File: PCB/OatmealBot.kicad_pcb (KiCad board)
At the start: 2 copper layers, 65 x 56 mm, 12 parts, among them J2 RPi_GPIO, J5 Motor 3, J6 Motor 4, J8 Motor 1, J9 Motor 2, U2 SPI_OLED, U3 FTDI-Cable, U4 PololuD24V22F

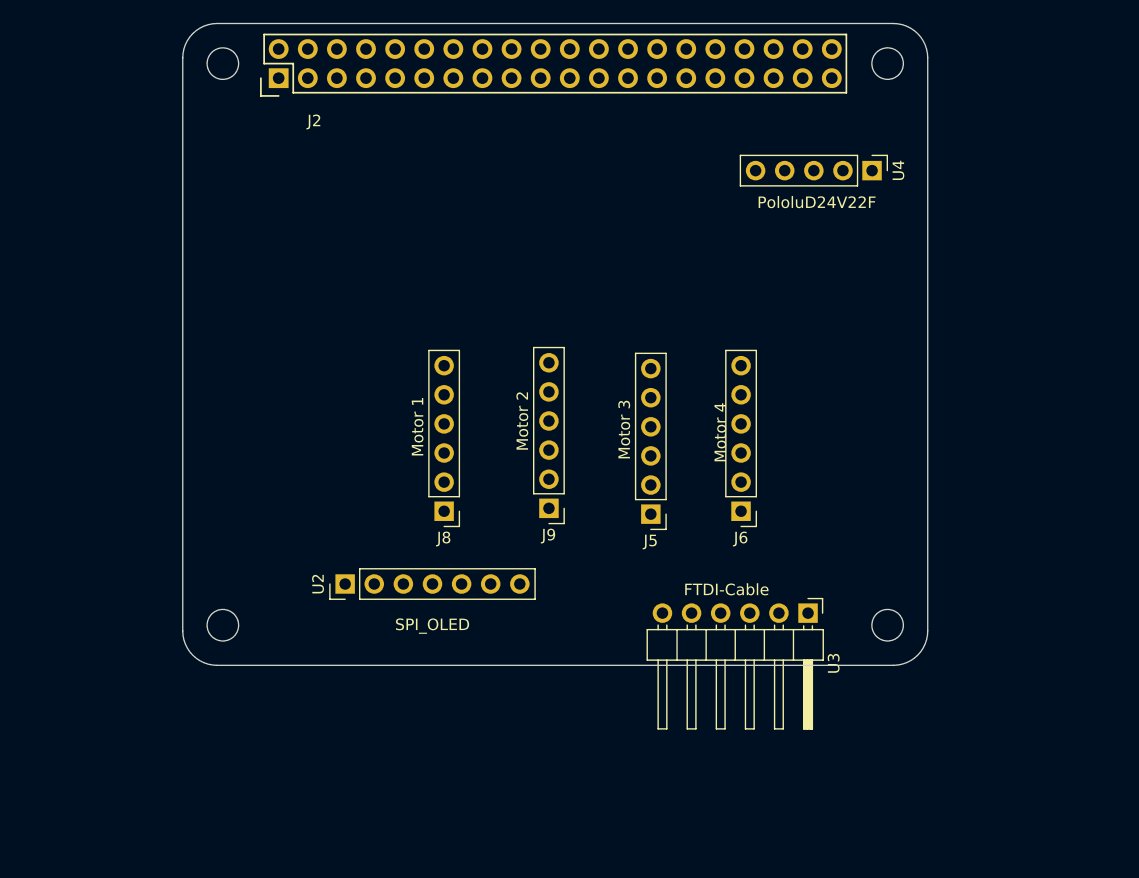
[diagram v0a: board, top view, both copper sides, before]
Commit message: Updated to KiCad 4.0.7 (which lost the 3D models I had just gotten working) Assigned more footprints.
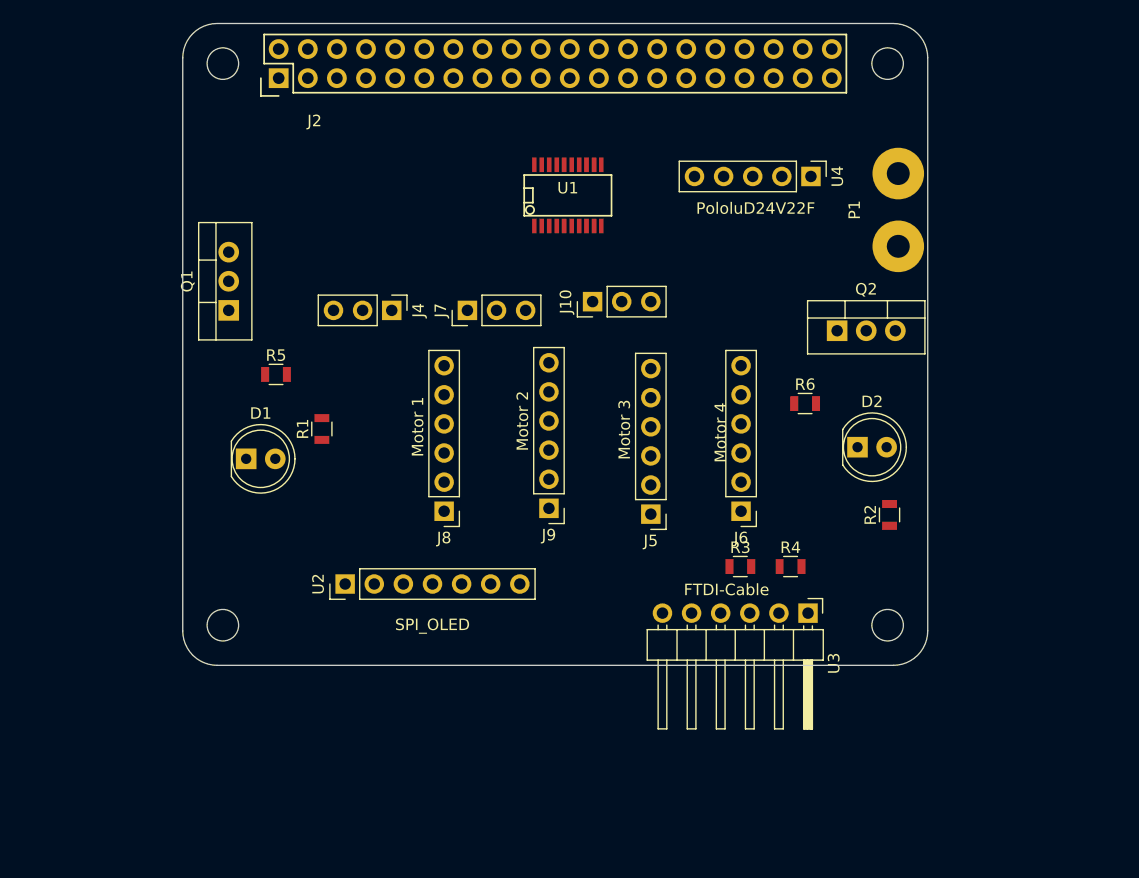
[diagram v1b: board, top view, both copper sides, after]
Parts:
- added D1: LED, LEDs:LED_D5.0mm, F.Cu at (18.0, 62.5)
- added D2: LED, LEDs:LED_D5.0mm, F.Cu at (71.4, 61.5)
- added J10: ServoHeader3, Pin_Headers:Pin_Header_Straight_1x03_Pitch2.54mm, F.Cu at (48.3, 48.8)
- added J4: ServoHeader1, Pin_Headers:Pin_Header_Straight_1x03_Pitch2.54mm, F.Cu at (30.7, 49.5)
- added J7: ServoHeader2, Pin_Headers:Pin_Header_Straight_1x03_Pitch2.54mm, F.Cu at (37.3, 49.5)
- added P1: Motor Hat Power, Wire_Pads:SolderWirePad_2x_2mmDrill, F.Cu at (74.9, 40.8)
- added Q1: STP55NF06L, TO_SOT_Packages_THT:TO-220-3_Vertical, F.Cu at (16.5, 49.5)
- added Q2: STP55NF06L, TO_SOT_Packages_THT:TO-220-3_Vertical, F.Cu at (69.6, 51.3)
- added R1: 330, Resistors_SMD:R_0805, F.Cu at (24.6, 59.9)
- added R2: 330, Resistors_SMD:R_0805, F.Cu at (74.2, 67.4)
- added R3: R, Resistors_SMD:R_0805, F.Cu at (61.1, 71.9)
- added R4: R, Resistors_SMD:R_0805, F.Cu at (65.5, 71.9)
- added R5: 10K, Resistors_SMD:R_0805, F.Cu at (20.6, 55.1)
- added R6: 10K, Resistors_SMD:R_0805, F.Cu at (66.8, 57.7)
- added U1: 74LVC245A, SMD_Packages:SSOP-20, F.Cu at (46.1, 39.5)
- moved U4 5.36 mm to (67.3, 37.8)

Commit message: Created proper footprint for the voltage regulator so it's easier to see how much space it takes up on the board. Changed the board layout to fit the regulator. Fixed some more 3D files
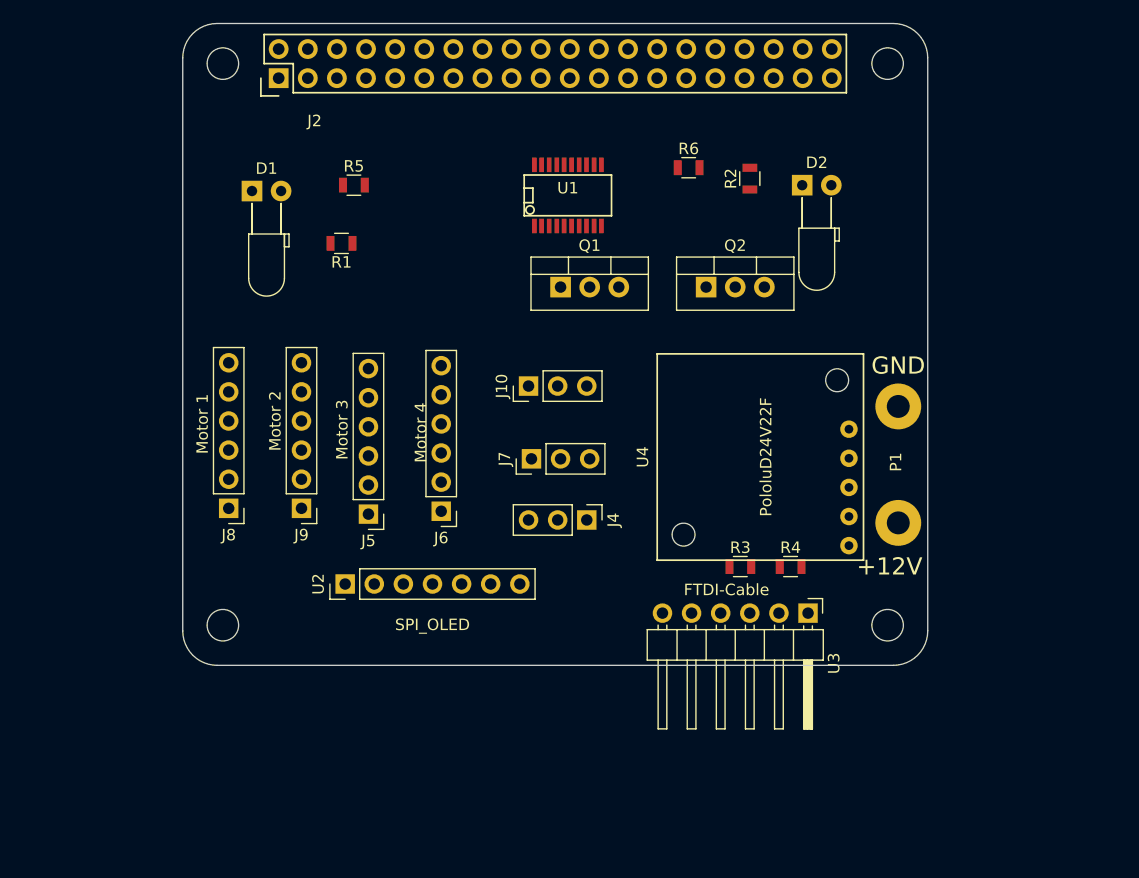
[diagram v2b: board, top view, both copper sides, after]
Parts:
- D1, D2: footprint LEDs:LED_D5.0mm -> LEDs:LED_D3.0mm_Horizontal_O3.81mm_Z10.0mm
- P1: footprint Wire_Pads:SolderWirePad_2x_2mmDrill -> Wire_Connections_Bridges:WireConnection_2.00mmDrill
- U4: footprint Socket_Strips:Socket_Strip_Straight_1x05_Pitch2.54mm -> schminktronics:PololuD24V22F
- moved R2 31.8 mm to (62.0, 38.0)
- moved Q1 29.0 mm to (45.5, 47.5), turned to 0 degrees
- moved J6 26.2 mm to (35.1, 67.1)
- moved J4 25.0 mm to (47.8, 67.8)
- moved U4 24.9 mm to (62.9, 62.3)
- moved J5 24.6 mm to (28.7, 67.3)
- moved D1 23.4 mm to (18.5, 39.1)
- moved D2 23.4 mm to (66.5, 38.6)
- moved R6 22.9 mm to (56.6, 37.1)
- moved J9 21.6 mm to (22.9, 66.8)
- moved J8 18.8 mm to (16.5, 66.8)
- moved R5 17.9 mm to (27.4, 38.6)
- moved P1 17.1 mm to (74.9, 57.9), turned to 270 degrees
- moved R1 16.3 mm to (26.4, 43.7), turned to 180 degrees
- moved J7 14.1 mm to (42.9, 62.5)
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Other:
- board text added: "+12V"
- board text added: "GND"

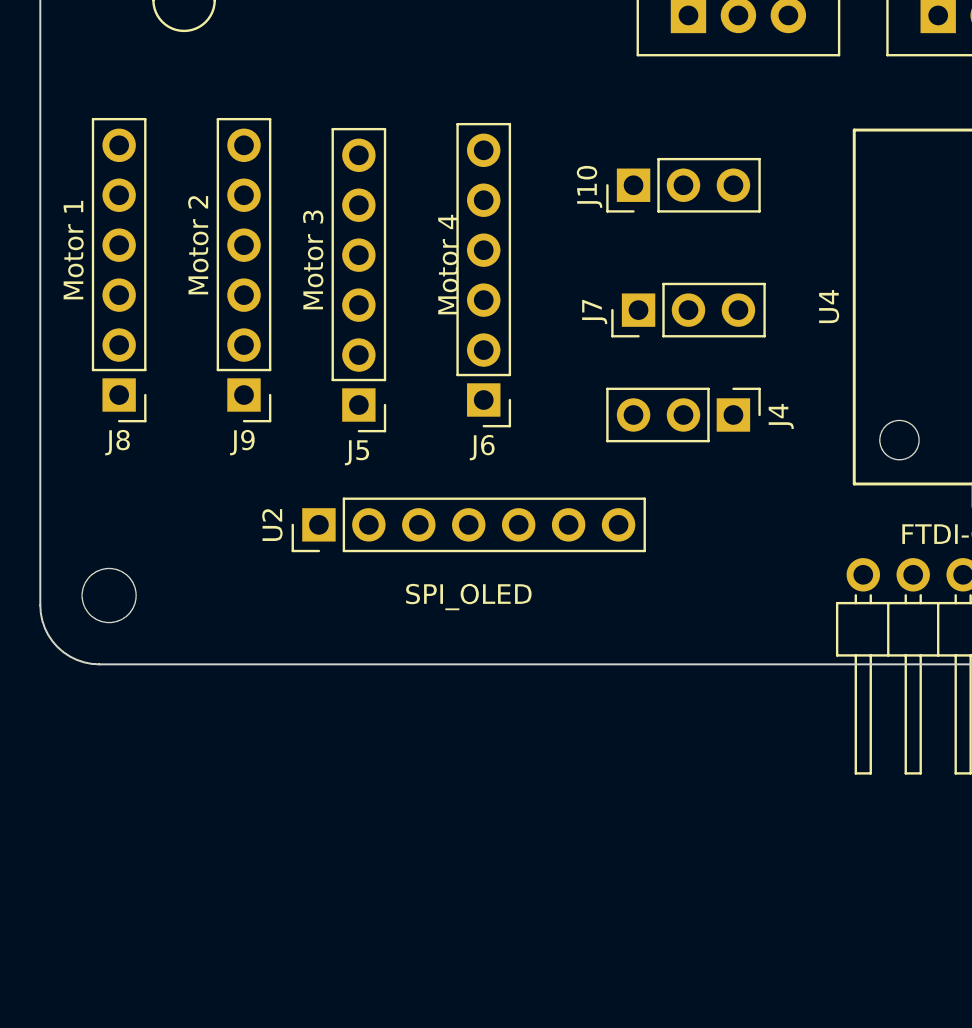
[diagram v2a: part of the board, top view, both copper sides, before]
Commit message: Started work on the board layout.
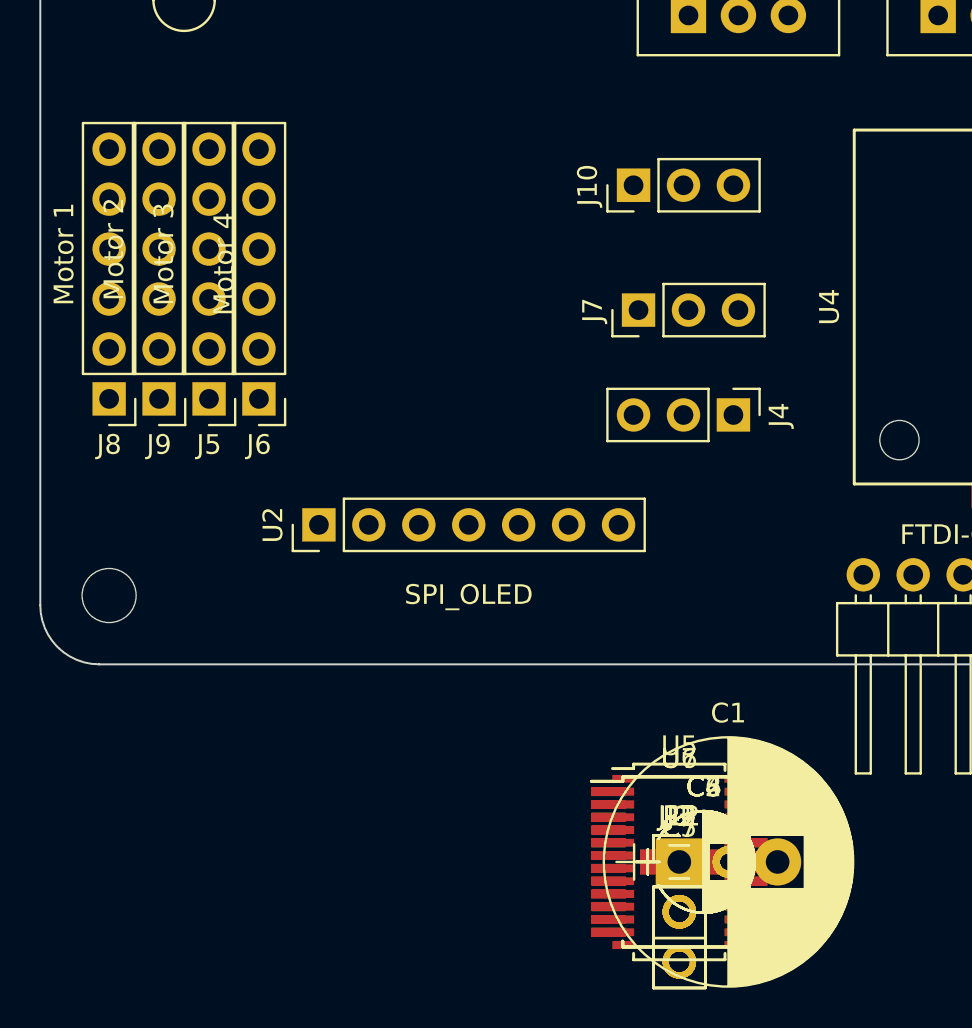
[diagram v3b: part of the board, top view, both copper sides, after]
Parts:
- added C1: 470uF, Capacitors_ThroughHole:CP_Radial_D12.5mm_P5.00mm, F.Cu at (45.0, 90.6)
- added C2, C4: 10uF, Capacitors_ThroughHole:CP_Radial_D5.0mm_P2.50mm, F.Cu at (45.0, 90.6)
- added C3, C6: 47uF, Capacitors_ThroughHole:CP_Radial_D5.0mm_P2.50mm, F.Cu at (45.0, 90.6)
- added C5, C7: 0.1uF, Capacitors_SMD:C_0805_HandSoldering, F.Cu at (45.0, 90.6)
- added J1: ServoHeader1, Pin_Headers:Pin_Header_Straight_1x03_Pitch2.54mm, F.Cu at (45.0, 90.6)
- added J11, J12: ServoHeader3, Pin_Headers:Pin_Header_Straight_1x03_Pitch2.54mm, F.Cu at (45.0, 90.6)
- added J3: ServoHeader2, Pin_Headers:Pin_Header_Straight_1x03_Pitch2.54mm, F.Cu at (45.0, 90.6)
- added P2: HighPower2, Pin_Headers:Pin_Header_Straight_1x02_Pitch2.54mm, F.Cu at (45.0, 90.6)
- added P3: Headlight, Pin_Headers:Pin_Header_Straight_1x02_Pitch2.54mm, F.Cu at (45.0, 90.6)
- added U5: PCA9685, Housings_SSOP:TSSOP-28_4.4x9.7mm_Pitch0.65mm, F.Cu at (45.0, 90.6)
- added U6, U7: TB6612FNG, Housings_SSOP:SSOP-24_5.3x8.2mm_Pitch0.65mm, F.Cu at (45.0, 90.6)
- D1: value LED -> Status LED
- D2: value LED -> Error LED
- moved J6 11.4 mm to (23.6, 67.0)
- moved J5 7.63 mm to (21.1, 67.0)
- moved J9 4.32 mm to (18.5, 67.0)
- moved J8 0.55 mm to (16.0, 67.0)
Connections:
- J2 pad 1: +3.3V -> +3V3
- J2 pad 17: +3.3V -> +3V3
- J2 pad 3: Net-(J2-Pad3) -> SDA
- J2 pad 5: Net-(J2-Pad5) -> SCL
- J5 pad 1: Net-(J3-Pad1) -> /MotorController/Motor3+
- J5 pad 2: Net-(J3-Pad2) -> /MotorController/Motor3-
- J6 pad 1: Net-(J3-Pad4) -> /MotorController/Motor4+
- J6 pad 2: Net-(J3-Pad5) -> /MotorController/Motor4-
- J8 pad 1: Net-(J1-Pad1) -> /MotorController/Motor1+
- J8 pad 2: Net-(J1-Pad2) -> /MotorController/Motor1-
- J9 pad 1: Net-(J1-Pad4) -> /MotorController/Motor2+
- J9 pad 2: Net-(J1-Pad5) -> /MotorController/Motor2-
- U1 pad 1: +3.3V -> +3V3
- U1 pad 20: +3.3V -> +3V3

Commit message: Initial lay out of servo headers and all components.
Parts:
- J1: value ServoHeader1 -> 4
- J10: value ServoHeader3 -> 3
- J11: value ServoHeader3 -> 6
- J12: value ServoHeader3 -> 7
- J3: value ServoHeader2 -> 5
- J4: value ServoHeader1 -> 1
- J5: value Motor 3 -> 3
- J6: value Motor 4 -> 4
- J7: value ServoHeader2 -> 2
- J8: value Motor 1 -> 1
- J9: value Motor 2 -> 2
- U1, U6, U7: moved to B.Cu
- moved U5 54.7 mm to (37.9, 36.3), turned to 90 degrees
- moved C1 52.6 mm to (49.5, 38.1)
- moved P3 42.9 mm to (63.1, 51.7), turned to 270 degrees
- moved P2 39.2 mm to (50.6, 51.7), turned to 270 degrees
- moved J1 32.0 mm to (37.6, 59.4), turned to 180 degrees
- moved J3 31.5 mm to (40.2, 59.4), turned to 180 degrees
- moved J11 31.3 mm to (42.7, 59.4), turned to 180 degrees
- moved J12 31.2 mm to (45.2, 59.4), turned to 180 degrees
- moved U6 30.3 mm to (18.8, 75.5), turned to 270 degrees
- moved C7 28.4 mm to (20.8, 75.6), turned to 90 degrees
- moved U1 27.9 mm to (19.8, 48.8)
- moved C2 27.8 mm to (30.5, 66.8)
- moved C3 24.9 mm to (37.4, 66.8)
- moved C6 23.7 mm to (49.9, 67.4)
- moved C4 23.0 mm to (43.8, 67.5)
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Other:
- board text added: "Motors"

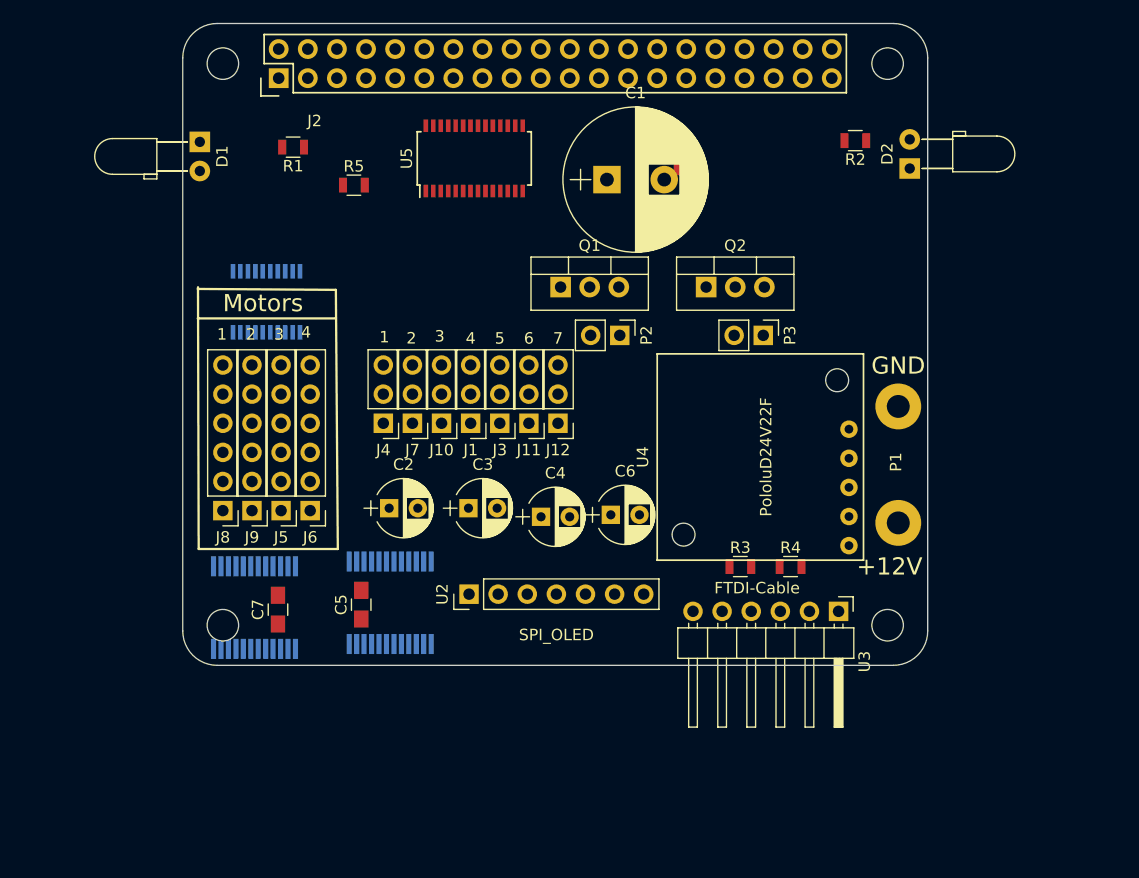
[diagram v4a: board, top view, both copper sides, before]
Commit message: Footprint changes and board layout changes
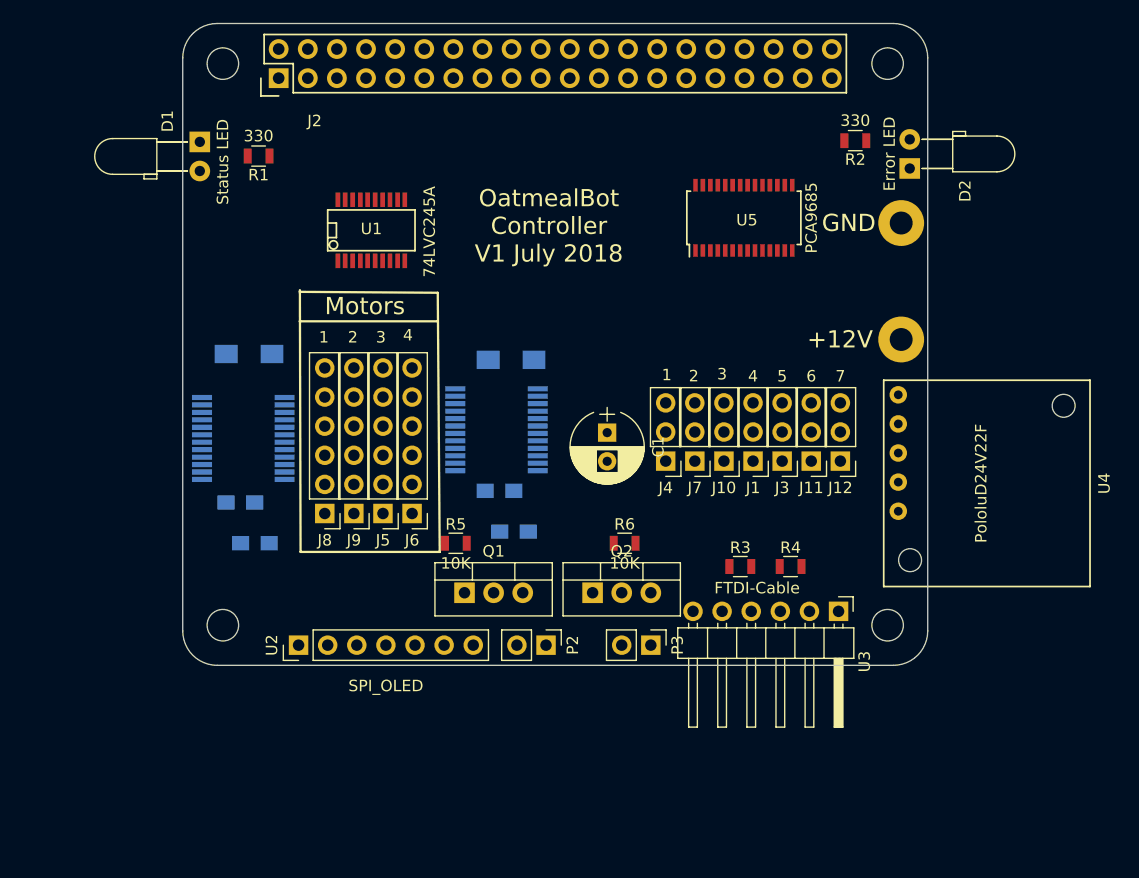
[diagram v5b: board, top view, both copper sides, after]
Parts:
- C1: value 470uF -> 330uF; footprint Capacitors_ThroughHole:CP_Radial_D12.5mm_P5.00mm -> Capacitors_ThroughHole:CP_Radial_D6.3mm_P2.50mm
- C2, C4: footprint Capacitors_ThroughHole:CP_Radial_D5.0mm_P2.50mm -> Capacitors_SMD:C_0805_HandSoldering; moved to B.Cu
- C3, C6: footprint Capacitors_ThroughHole:CP_Radial_D5.0mm_P2.50mm -> Capacitors_SMD:C_1206_HandSoldering; moved to B.Cu
- C5, C7: moved to B.Cu
- U1: moved to F.Cu
- moved R6 33.2 mm to (51.1, 69.8)
- moved R5 32.5 mm to (36.3, 69.8)
- moved P3 28.8 mm to (53.3, 78.7)
- moved Q2 28.5 mm to (48.3, 74.2)
- moved Q1 28.0 mm to (37.1, 74.2)
- moved P2 27.8 mm to (44.2, 78.7)
- moved J1 24.9 mm to (62.3, 62.7)
- moved J10 24.9 mm to (59.7, 62.7)
- moved J3 24.9 mm to (64.8, 62.7)
- moved J12 24.9 mm to (69.9, 62.7)
- moved J4 24.9 mm to (54.6, 62.7)
- moved J7 24.9 mm to (57.2, 62.7)
- moved J11 24.9 mm to (67.3, 62.7)
- moved U5 24.1 mm to (61.5, 41.5)
- moved C3 23.4 mm to (18.3, 53.3), turned to 180 degrees
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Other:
- board text added: "OatmealBot Controller V1 July 2018"
